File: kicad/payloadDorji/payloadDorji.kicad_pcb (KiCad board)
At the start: 2 copper layers, 79.8 x 79.8 mm, 49 parts, among them J1 Conn_01x01_Pin, J1 PWR, J2 Conn_Coaxial, J3 Conn_01x06_Male, J4 PWR, J5 UART, U1 LM386, U2 DRA818V, U3 MAX-M10M-00B, U4 NUCLEO-L432KC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

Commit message: mounting holes, vias, etc
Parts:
- added REF**: MountingHole_4.3mm_M4, MountingHole:MountingHole_4.3mm_M4, F.Cu at (196.0, 21.0)
- added REF**: MountingHole_4.3mm_M4, MountingHole:MountingHole_4.3mm_M4, F.Cu at (120.0, 22.0)
- L5: footprint Inductor_THT:L_Axial_L5.0mm_D3.6mm_P10.00mm_Horizontal_Murata_BL01RN1A2A2 -> Inductor_SMD:L_1008_2520Metric
- moved L5 4.21 mm to (174.6, 75.6)
- moved C16 3.56 mm to (199.5, 74.9)
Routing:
- net +3.3V: track 200.9 -> 205.3 mm
- net Net-(U5-SW): track 6.49 -> 10.1 mm
- net GND: track 49.2 -> 45.9 mm, vias 42 -> 31
- net +BATT: track 35.2 -> 36.5 mm
- net GPS_UART_TX: track 38.0 -> 38.6 mm
- net GPS_UART_RX: track 21.1 -> 21.6 mm
- net +5V: vias 2 -> 1
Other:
- board size 79.8 x 79.8 mm -> 85.9 x 85.9 mm

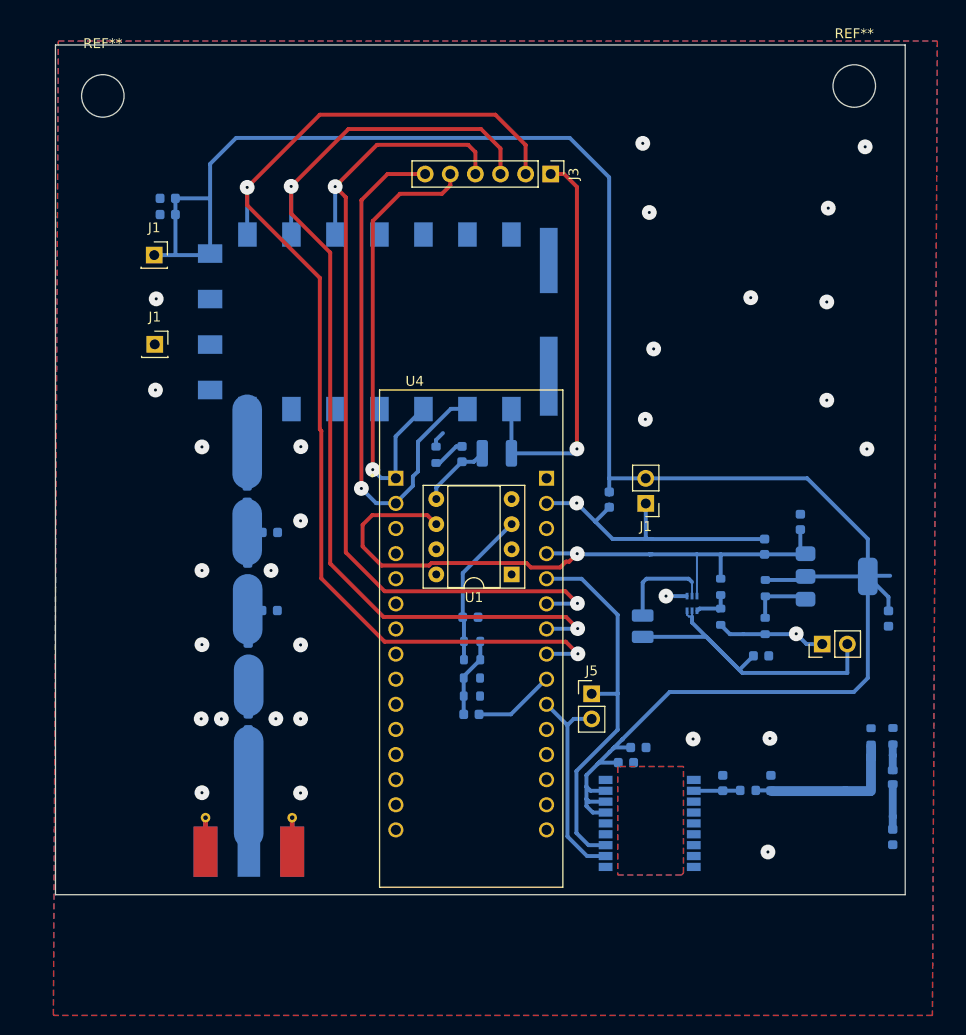
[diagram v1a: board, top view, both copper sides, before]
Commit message: kiCAD cleanup! Added .gitignore file, removed temporary files from git, fixed library paths to be relative, cleaned up schematic errors, cleaned up layout errors, cleaned up consistency between sch/brd.
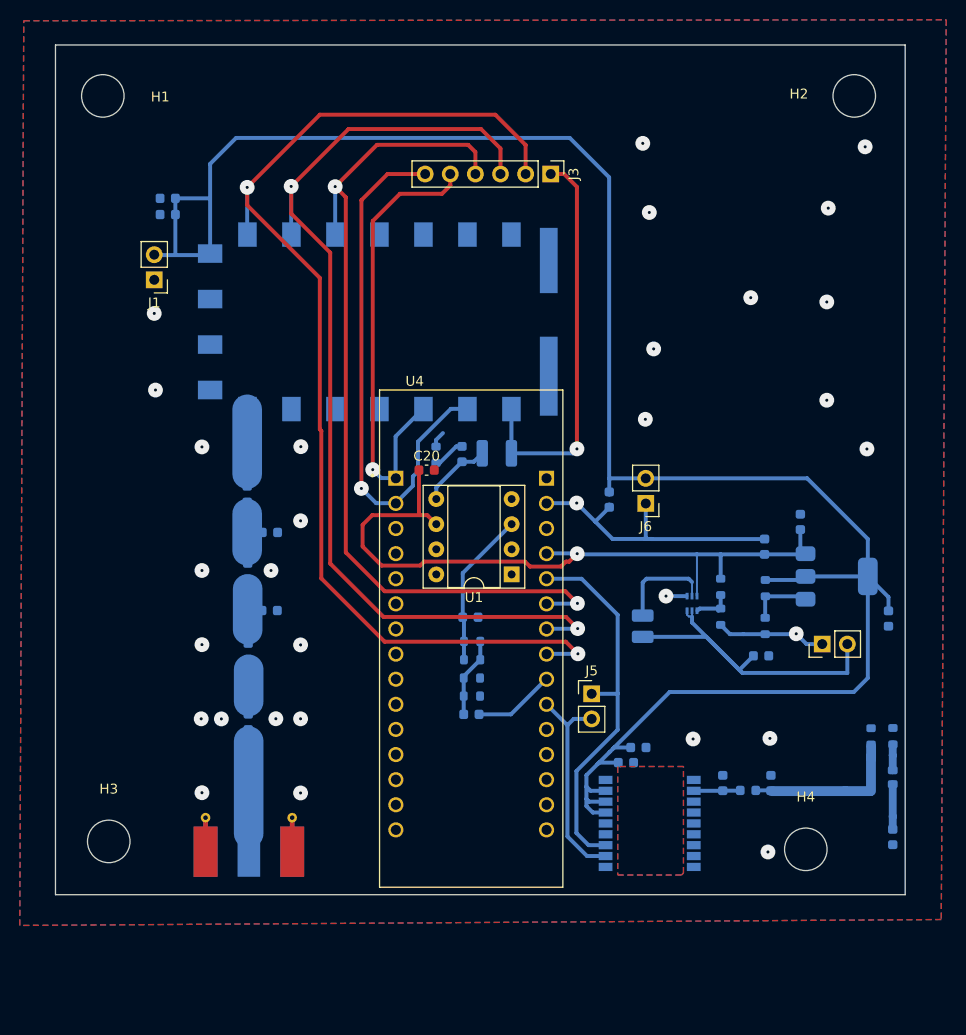
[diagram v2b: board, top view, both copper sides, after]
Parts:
- removed the J1 at (125.2, 47.1)
- removed REF**: MountingHole_4.3mm_M4, MountingHole:MountingHole_4.3mm_M4
- added C20: 100n, Capacitor_SMD:C_0603_1608Metric, F.Cu at (152.8, 59.9)
- added H2: MountingHole, MountingHole:MountingHole_4.3mm_M4, F.Cu at (196.0, 22.0)
- added H3: MountingHole, MountingHole:MountingHole_4.3mm_M4, F.Cu at (120.6, 97.4)
- added H4: MountingHole, MountingHole:MountingHole_4.3mm_M4, F.Cu at (191.1, 98.2)
- H1: renamed from REF**; value MountingHole_4.3mm_M4 -> MountingHole
- J1: value Conn_01x01_Pin -> PWR; footprint Connector_PinSocket_2.54mm:PinSocket_1x01_P2.54mm_Vertical -> Connector_PinHeader_2.54mm:PinHeader_1x02_P2.54mm_Vertical
- moved J1 2.50 mm to (125.2, 40.6), turned to 180 degrees
- renumbered J1 to J6
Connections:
- net /MIC_IN renamed MIC_IN
- J1 pad 1: +3.3V -> GND
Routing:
- net +5V: track 69.9 -> 74.2 mm
- net +3.3V: track 205.3 -> 202.9 mm

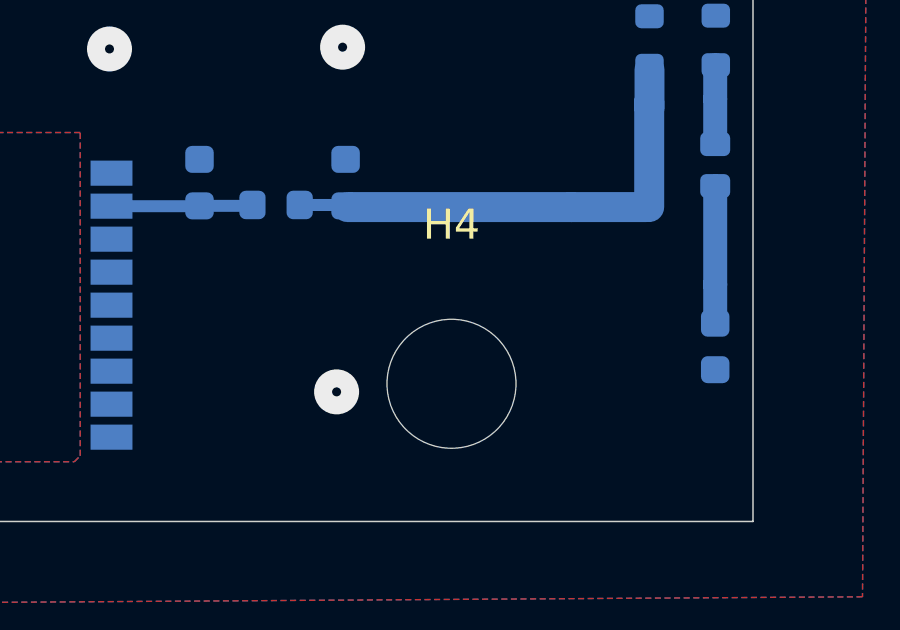
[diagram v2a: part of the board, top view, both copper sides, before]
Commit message: Fixed library paths. Add PICOAPRS_LIBRARIES to your project variables which points to the kicad/lib directory. Also fixed up schematic to be more readable, and fixed some more issues between sch/brd.
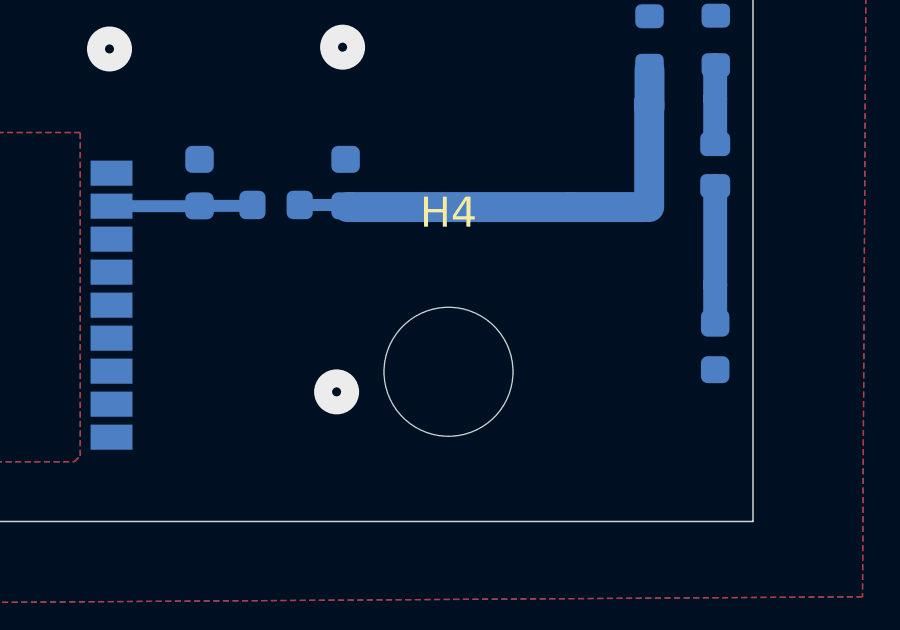
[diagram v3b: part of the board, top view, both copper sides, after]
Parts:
- C1, C2: value 0.1u -> 100n
- C11, C12: value DNP -> ~
- C3: value 0.05u -> 50n
- U5: footprint footprints:DRL0006A -> picoaprs:DRL0006A
- moved H4 0.41 mm to (191.0, 97.8)
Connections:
- net MIC_IN renamed /MIC_IN
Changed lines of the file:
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@@
 	(net 4 "Net-(C3-Pad1)")
 	(net 5 "Net-(C3-Pad2)")
-	(net 6 "MIC_IN")
+	(net 6 "/MIC_IN")
 	(net 7 "Net-(U2-ANT)")
 	(net 8 "Net-(C6-Pad1)")
@@
 	(footprint "MountingHole:MountingHole_4.3mm_M4"
 		(layer "F.Cu")
-		(at 191.1 98.2)
+		(at 191 97.8)
 		(descr "Mounting Hole 4.3mm, no annular, M4")
 		(tags "mounting hole 4.3mm no annular m4")
@@
 			(layers "*.Cu" "*.Mask")
 			(remove_unused_layers no)
-			(net 6 "MIC_IN")
+			(net 6 "/MIC_IN")
 			(pinfunction "Pin_1")
 			(pintype "passive")
@@
 		(tags "Through hole pin header THT 1x02 2.54mm single row")
 		(property "Reference" "J1"
-			(at 0 -2.33 360)
+			(at 0 -2.33 0)
 			(layer "F.SilkS")
 			(effects
@@
 		)
 		(property "Value" "PWR"
-			(at 0 4.87 360)
+			(at 0 4.87 0)
 			(layer "F.Fab")
 			(effects
@@
 			)
 		)
-		(property "Value" "0.1u"
+		(property "Value" "100n"
 			(at 0 -1.43 0)
 			(layer "B.Fab")
@@
 			(layers "B.Cu" "B.Paste" "B.Mask")
 			(roundrect_rratio 0.217391)
-			(net 6 "MIC_IN")
+			(net 6 "/MIC_IN")
 			(pintype "passive")
 		)
@@
 		)
 	)
-	(footprint "footprints:DRL0006A"
+	(footprint "picoaprs:DRL0006A"
 		(layer "B.Cu")
 		(at 179.59 73.33 90)
@@
 			)
 		)
-		(property "Footprint" "footprints:DRL0006A"
-			(at 0 0 90)
+		(property "Footprint" "DRL0006A"
+			(at 0 0 -90)
 			(layer "B.Fab")
 			(hide yes)
@@
 			)
 		)
-		(property "Datasheet" "TPS61023DRLR"
-			(at 0 0 90)
+		(property "Datasheet" "https://www.ti.com/lit/ds/symlink/tps61023.pdf"
+			(at 0 0 -90)
 			(layer "B.Fab")
 			(hide yes)
@@
 		)
 		(property "Description" ""
-			(at 0 0 90)
+			(at 0 0 -90)
 			(layer "B.Fab")
 			(hide yes)
@@
 			(net 28 "Net-(U5-SW)")
 			(pinfunction "SW")
-			(pintype "power_in")
+			(pintype "passive")
 		)
 		(pad "6" smd rect
@@
 			(net 12 "+5V")
 			(pinfunction "VOUT")
-			(pintype "power_in")
+			(pintype "power_out")
 		)
 	)
@@
 			)
 		)
-		(property "Value" "0.05u"
+		(property "Value" "50n"
 			(at 0 -1.43 90)
 			(layer "B.Fab")
@@
 			)
 		)
-		(property "Value" "DNP"
+		(property "Value" "~"
 			(at 0 -1.43 90)
 			(layer "B.Fab")
@@
 		(sheetname "Root")
 		(sheetfile "payloadDorji.kicad_sch")
-		(attr smd)
+		(attr smd exclude_from_bom dnp)
 		(fp_line
 			(start 0.14058 0.51)
@@
 			(size 2.47 1.88)
 			(layers "B.Cu" "B.Paste" "B.Mask")
-			(net 6 "MIC_IN")
+			(net 6 "/MIC_IN")
 			(pinfunction "MIC_IN")
 			(pintype "input")
@@
 			)
 		)
-		(property "Value" "DNP"
+		(property "Value" "~"
 			(at 0 -1.43 90)
 			(layer "B.Fab")
@@
 		(sheetname "Root")
 		(sheetfile "payloadDorji.kicad_sch")
-		(attr smd)
+		(attr smd exclude_from_bom dnp)
 		(fp_line
 			(start 0.14058 0.51)
@@
 			)
 		)
-		(property "Value" "0.1u"
+		(property "Value" "100n"
 			(at 0 -1.43 0)
 			(layer "B.Fab")

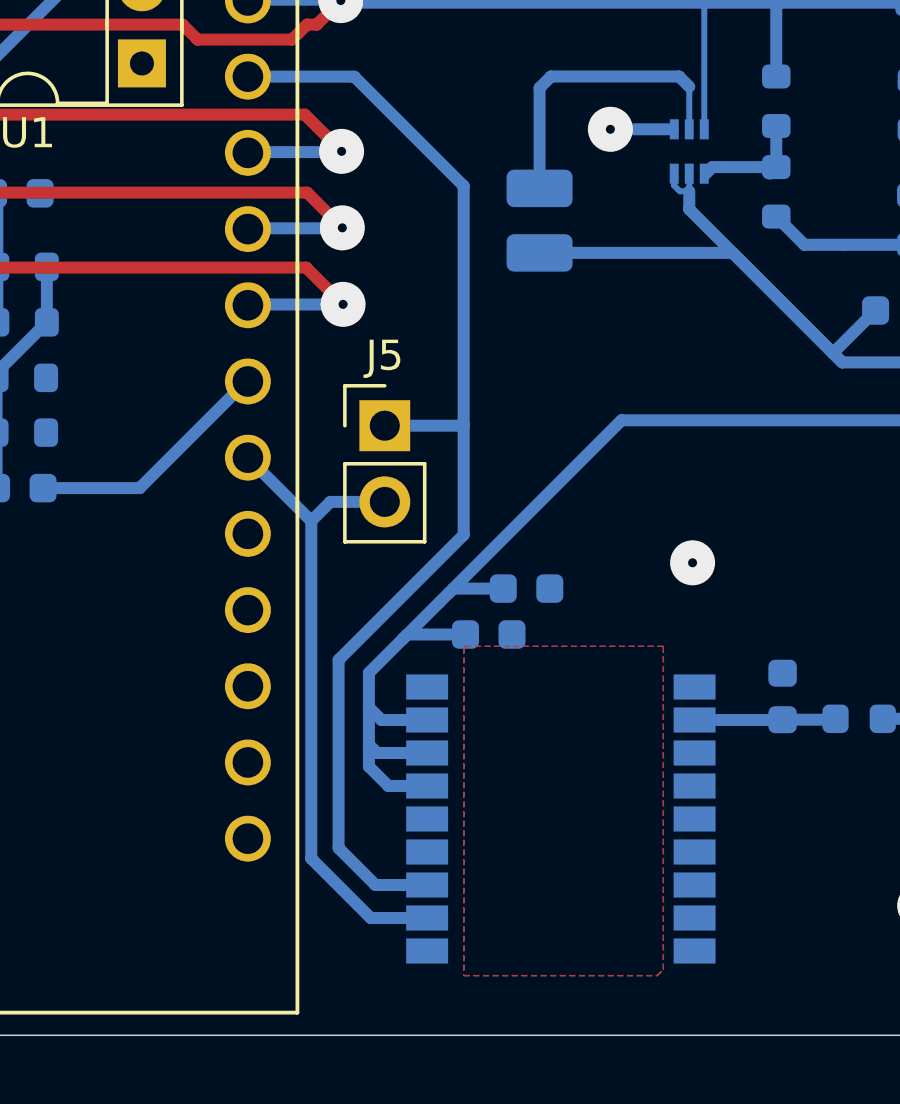
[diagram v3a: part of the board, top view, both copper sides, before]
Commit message: Fixed GPS symbol (blech) and found two misconnected pins. Fixed in shcematic and layout.
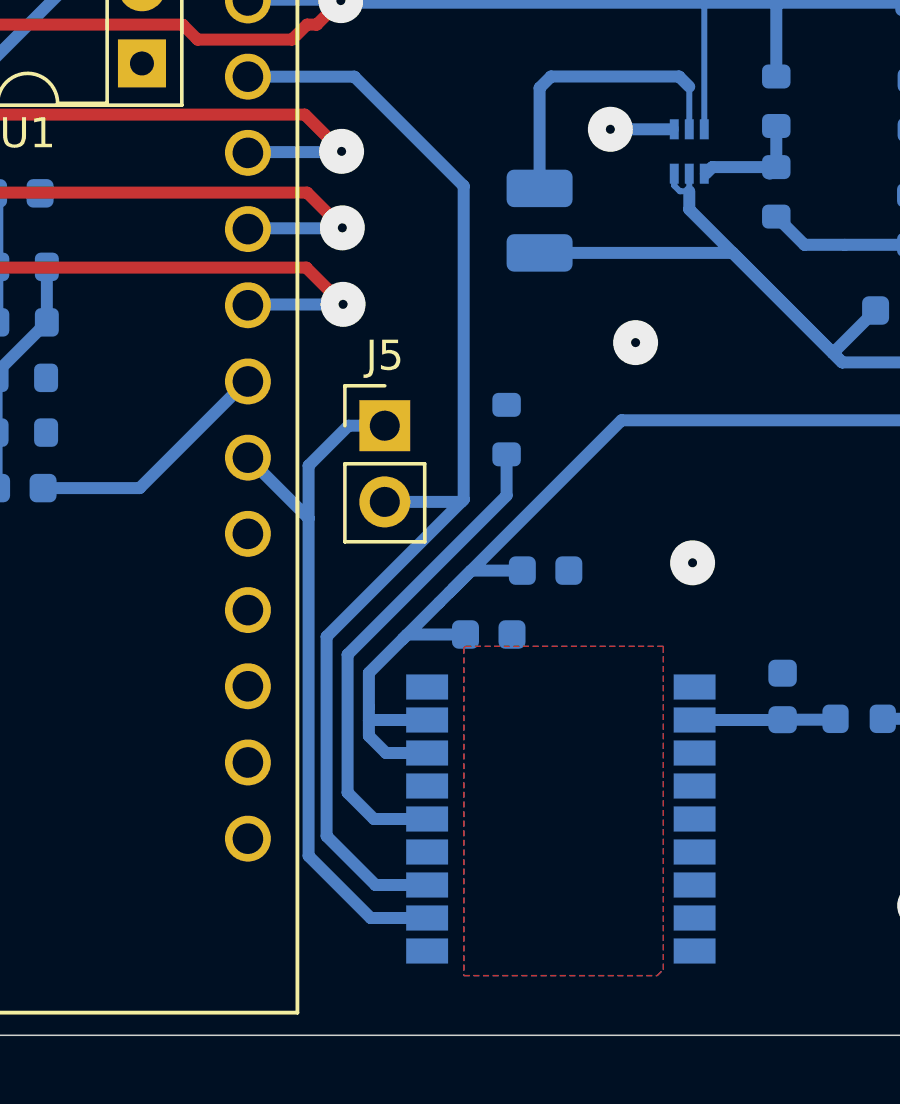
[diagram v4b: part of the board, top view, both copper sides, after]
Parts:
- added R12: 3.3k, Resistor_SMD:R_0603_1608Metric, B.Cu at (173.5, 82.6)
- U3: footprint footprints:MOD18_MAX-M10M_UBL -> picoaprs:MOD18_MAX-M10M_UBL
- moved C9 0.87 mm to (174.8, 87.3)
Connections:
- net /H/L renamed H/L
- net /PD renamed PD
- net /PTT renamed PTT
- U3 pad 2: GPS_UART_RX -> GPS_UART_TX
- U3 pad 3: GPS_UART_TX -> GPS_UART_RX
- U3 pad 5: unconnected-(U3-EXTINT-Pad5) -> Net-(U3-EXTINT)
- U3 pad 6: +3.3V -> unconnected-(U3-V_BCKP-Pad6)
- U4 pad CN4_10: GPS_UART_RX -> GPS_UART_TX
- U4 pad CN4_5: GPS_UART_TX -> GPS_UART_RX
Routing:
- net GPS_UART_RX: track 21.6 -> 39.0 mm
- net Net-(U3-EXTINT): track 0.00 -> 16.5 mm
- net GPS_UART_TX: track 38.6 -> 23.8 mm
- net +3.3V: track 202.9 -> 200.5 mm
- net GND: vias 31 -> 32

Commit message: Fix final missing footprints! OK, NOW everything is fixed.
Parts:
- AE1: footprint PicoAPRS-CustomFootprints:AC30157-01 GNSS Ceramic Chip -> picoaprs:AC30157-01 GNSS Ceramic Chip
- U2: footprint PicoAPRS-CustomFootprints:DORJI_DRA818V -> picoaprs:DORJI_DRA818V
- U4: footprint NUCLEO-L432KC:MODULE_NUCLEO-L432KC -> picoaprs:MODULE_NUCLEO-L432KC
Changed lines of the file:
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@@
 		)
 	)
-	(footprint "NUCLEO-L432KC:MODULE_NUCLEO-L432KC"
+	(footprint "picoaprs:MODULE_NUCLEO-L432KC"
 		(layer "F.Cu")
 		(at 157.2575 76.89)
@@
 			)
 		)
-		(property "Footprint" "NUCLEO-L432KC:MODULE_NUCLEO-L432KC"
+		(property "Footprint" "picoaprs:MODULE_NUCLEO-L432KC"
 			(at 0 0 0)
 			(layer "F.Fab")
@@
 			)
 		)
-		(property "Footprint" "MOD18_MAX-M10M_UBL"
+		(property "Footprint" "picoaprs:MOD18_MAX-M10M_UBL"
 			(at 0 0 180)
 			(layer "B.Fab")
@@
 		)
 	)
-	(footprint "PicoAPRS-CustomFootprints:AC30157-01 GNSS Ceramic Chip"
+	(footprint "picoaprs:AC30157-01 GNSS Ceramic Chip"
 		(layer "B.Cu")
 		(at 197.59 91.81 90)
 		(property "Reference" "AE1"
-			(at 5.01 -2.19 -90)
+			(at 0 3.7 -90)
 			(unlocked yes)
 			(layer "B.SilkS")
@@
 			)
 		)
-		(property "Footprint" "PicoAPRS-CustomFootprints:AC30157-01 GNSS Ceramic Chip"
+		(property "Footprint" "picoaprs:AC30157-01 GNSS Ceramic Chip"
 			(at 0.9 1.8 -90)
 			(unlocked yes)
@@
 		)
 	)
-	(footprint "PicoAPRS-CustomFootprints:DORJI_DRA818V"
+	(footprint "picoaprs:DORJI_DRA818V"
 		(layer "B.Cu")
 		(at 147.975 44.8475 180)
@@
 			)
 		)
-		(property "Footprint" "PicoAPRS-CustomFootprints:DORJI_DRA818V"
+		(property "Footprint" "picoaprs:DORJI_DRA818V"
 			(at 0 0 0)
 			(layer "B.Fab")
@@
 		)
 		(property "MF" "DORJI"
-			(at 0 0 0)
+			(at 0 0 180)
 			(unlocked yes)
 			(layer "B.Fab")
@@
 		)
 		(property "Description_1" "\n"
-			(at 0 0 0)
+			(at 0 0 180)
 			(unlocked yes)
 			(layer "B.Fab")
@@
 		)
 		(property "Package" "Package"
-			(at 0 0 0)
+			(at 0 0 180)
 			(unlocked yes)
 			(layer "B.Fab")
@@
 		)
 		(property "Price" "None"
-			(at 0 0 0)
+			(at 0 0 180)
 			(unlocked yes)
 			(layer "B.Fab")
@@
 		)
 		(property "Check_prices" "https://www.snapeda.com/parts/DRA818V/DORJI/view-part/?ref=eda"
-			(at 0 0 0)
+			(at 0 0 180)
 			(unlocked yes)
 			(layer "B.Fab")
@@
 		)
 		(property "PART_REV" "1.23"
-			(at 0 0 0)
+			(at 0 0 180)
 			(unlocked yes)
 			(layer "B.Fab")
@@
 		)
 		(property "STANDARD" "MANUFACTURER RECOMMENDATIONS"
-			(at 0 0 0)
+			(at 0 0 180)
 			(unlocked yes)
 			(layer "B.Fab")
@@
 		)
 		(property "SnapEDA_Link" "https://www.snapeda.com/parts/DRA818V/DORJI/view-part/?ref=snap"
-			(at 0 0 0)
+			(at 0 0 180)
 			(unlocked yes)
 			(layer "B.Fab")
@@
 		)
 		(property "MP" "DRA818V"
-			(at 0 0 0)
+			(at 0 0 180)
 			(unlocked yes)
 			(layer "B.Fab")
@@
 		)
 		(property "Availability" "Not in stock"
-			(at 0 0 0)
+			(at 0 0 180)
 			(unlocked yes)
 			(layer "B.Fab")
@@
 		)
 		(property "MANUFACTURER" "DORJI"
-			(at 0 0 0)
+			(at 0 0 180)
 			(unlocked yes)
 			(layer "B.Fab")
